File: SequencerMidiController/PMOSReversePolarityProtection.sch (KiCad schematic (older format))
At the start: 4 parts, among them Q1 HX2301A

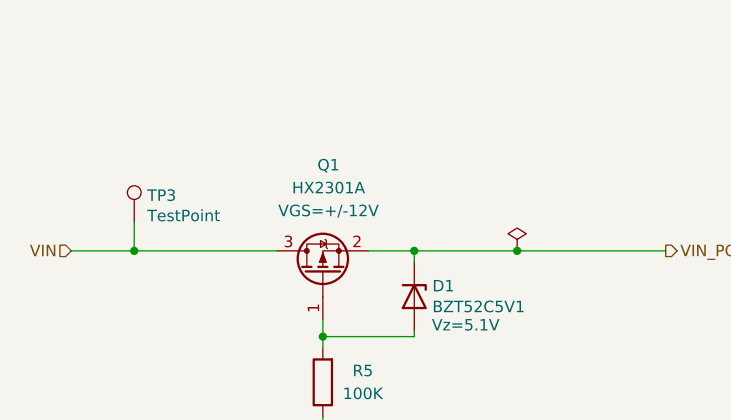
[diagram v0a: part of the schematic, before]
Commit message: RevA Layout draft completed
- Needs tidy up
- Add test points
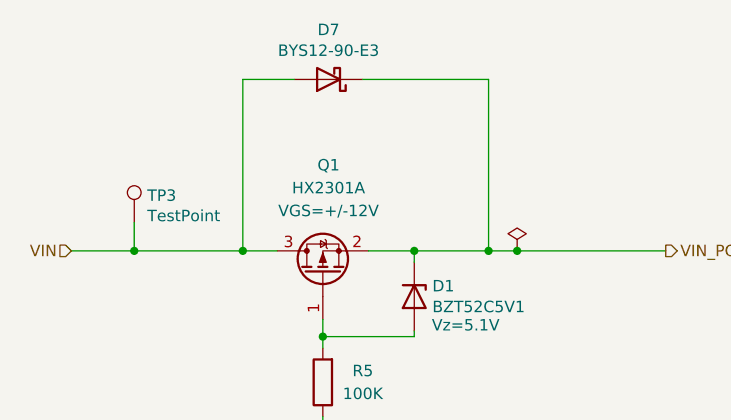
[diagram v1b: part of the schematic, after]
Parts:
- added D7: BYS12-90-E3, Diode_SMD:D_SMA, symbol Device:D_Schottky
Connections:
- net VIN: now also D7.2 (A)
- net VIN_POL: now also D7.1 (K)
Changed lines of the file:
@@
 Connection ~ 6100 2825
 Wire Wire Line
-	6100 2825 6550 2825
+	6100 2825 6425 2825
 Wire Wire Line
 	6100 2875 6100 2825
@@
 F 2 "Resistor_SMD:R_0805_2012Metric_Pad1.20x1.40mm_HandSolder" V 5630 3400 50  0001 C CNN
 F 3 "~" H 5700 3400 50  0001 C CNN
-F 4 "" V 5700 3400 50  0001 C CNN "Type"
-F 5 "" H 5700 3400 50  0001 C CNN "LcscNo"
+F 4 "~" V 5700 3400 50  0001 C CNN "Type"
+F 5 "~" H 5700 3400 50  0001 C CNN "LcscNo"
 	1    5700 3400
 	-1   0    0    1
@@
 $EndComp
 Wire Wire Line
-	5500 2825 4875 2825
+	5500 2825 5350 2825
 Text HLabel 4600 2825 0    50   Input ~ 0
 VIN
@@
 F 2 "TestPoint:TestPoint_Pad_1.0x1.0mm" H 5075 2700 50  0001 C CNN
 F 3 "~" H 5075 2700 50  0001 C CNN
+F 4 "~" H 4875 2700 50  0001 C CNN "LcscNo"
+F 5 "~" H 4875 2700 50  0001 C CNN "Type"
 	1    4875 2700
 	1    0    0    -1
@@
 Wire Wire Line
 	5700 3550 5700 3650
+$Comp
+L Device:D_Schottky D7
+U 1 1 634DDB6A
+P 5725 2075
+F 0 "D7" H 5725 1858 50  0000 C CNN
+F 1 "BYS12-90-E3" H 5725 1949 50  0000 C CNN
+F 2 "Diode_SMD:D_SMA" H 5725 2075 50  0001 C CNN
+F 3 "https://www.vishay.com/docs/88950/bys12-90.pdf" H 5725 2075 50  0001 C CNN
+	1    5725 2075
+	-1   0    0    1
+$EndComp
+Wire Wire Line
+	5575 2075 5350 2075
+Wire Wire Line
+	5350 2075 5350 2825
+Connection ~ 5350 2825
+Wire Wire Line
+	5350 2825 4875 2825
+Wire Wire Line
+	5875 2075 6425 2075
+Wire Wire Line
+	6425 2075 6425 2825
+Connection ~ 6425 2825
+Wire Wire Line
+	6425 2825 6550 2825
 $EndSCHEMATC

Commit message: Completed RevA layout
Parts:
- removed D7: BYS12-90-E3, Diode_SMD:D_SMA, symbol Device:D_Schottky
- D1: value BZT52C5V1 -> MMSZ4694T1G; LcscNo C353516 -> (none); Type Vz=5.1V -> (none)
- Q1: value HX2301A -> Si2323DS; symbol Transistor_FET:DMG2301L -> Device:Q_PMOS_GSD; Type VGS=+/-12V -> (none)
- R5: value 100K -> 100R
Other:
- note added: "RDS(ON) should be 100mΩ or less\nDrain current (4.5A) should be higher than 3A\nVDS (20V) should be higher than VIN (9V)"
- note added: "Zener Voltage should not exceed Q1 VGS limits"
- moved on the sheet: D1, Q1, R5, TP3
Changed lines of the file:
@@
 L power:PWR_FLAG #FLG?
 U 1 1 60B71BEE
-P 6550 2825
+P 8550 3825
 AR Path="/60B71BEE" Ref="#FLG?"  Part="1"
 AR Path="/5DEF0009/60B71BEE" Ref="#FLG?"  Part="1"
 AR Path="/60BD3123/60BD33F0/60B71BEE" Ref="#FLG0101"  Part="1"
-F 0 "#FLG0101" H 6550 2900 50  0001 C CNN
-F 1 "PWR_FLAG" H 6550 2996 50  0001 C CNN
-F 2 "" H 6550 2825 50  0001 C CNN
-F 3 "~" H 6550 2825 50  0001 C CNN
-	1    6550 2825
+F 0 "#FLG0101" H 8550 3900 50  0001 C CNN
+F 1 "PWR_FLAG" H 8550 3996 50  0001 C CNN
+F 2 "" H 8550 3825 50  0001 C CNN
+F 3 "~" H 8550 3825 50  0001 C CNN
+	1    8550 3825
 	1    0    0    -1
 $EndComp
-Connection ~ 6550 2825
+Connection ~ 8550 3825
 Wire Wire Line
-	6550 2825 7200 2825
+	8550 3825 9200 3825
 Wire Wire Line
-	5900 2825 6100 2825
-Connection ~ 6100 2825
+	5825 3825 6375 3825
+Connection ~ 6375 3825
 Wire Wire Line
-	6100 2825 6425 2825
+	6375 4125 6375 3825
 Wire Wire Line
-	6100 2875 6100 2825
+	5625 4450 5625 4125
+Connection ~ 5625 4450
 Wire Wire Line
-	5700 3200 5700 3125
-Connection ~ 5700 3200
+	6375 4450 5625 4450
 Wire Wire Line
-	6100 3200 5700 3200
-Wire Wire Line
-	6100 3175 6100 3200
+	6375 4425 6375 4450
 $Comp
 L Diode:BZT52Bxx D?
 U 1 1 60B71C00
-P 6100 3025
+P 6375 4275
 AR Path="/60B71C00" Ref="D?"  Part="1"
 AR Path="/5DEF0009/60B71C00" Ref="D?"  Part="1"
 AR Path="/60BD3123/60BD33F0/60B71C00" Ref="D1"  Part="1"
-F 0 "D1" V 6054 3104 50  0000 L CNN
-F 1 "BZT52C5V1" V 6145 3104 50  0000 L CNN
-F 2 "Diode_SMD:D_SOD-123" H 6100 2850 50  0001 C CNN
-F 3 "https://diotec.com/tl_files/diotec/files/pdf/datasheets/bzt52b2v4.pdf" H 6100 3025 50  0001 C CNN
-F 4 "Vz=5.1V" V 6225 3250 50  0000 C CNN "Type"
-F 5 "C353516" V 6100 3025 50  0001 C CNN "LcscNo"
-	1    6100 3025
+F 0 "D1" V 6329 4354 50  0000 L CNN
+F 1 "MMSZ4694T1G" V 6420 4354 50  0000 L CNN
+F 2 "Diode_SMD:D_SOD-123" H 6375 4100 50  0001 C CNN
+F 3 "https://www.onsemi.com/pdf/datasheet/mmsz4678t1-d.pdf" H 6375 4275 50  0001 C CNN
+F 4 "~" V 6500 4500 50  0001 C CNN "Type"
+F 5 "~" V 6375 4275 50  0001 C CNN "LcscNo"
+	1    6375 4275
 	0    1    1    0
 $EndComp
 Wire Wire Line
-	5700 3250 5700 3200
+	5625 4800 5625 4450
 $Comp
 L Device:R R?
 U 1 1 60B71C09
-P 5700 3400
+P 5625 4950
 AR Path="/60B71C09" Ref="R?"  Part="1"
 AR Path="/5DEF0009/60B71C09" Ref="R?"  Part="1"
 AR Path="/60BD3123/60BD33F0/60B71C09" Ref="R5"  Part="1"
-F 0 "R5" H 5525 3350 50  0000 C CNN
-F 1 "100K" H 5525 3450 50  0000 C CNN
-F 2 "Resistor_SMD:R_0805_2012Metric_Pad1.20x1.40mm_HandSolder" V 5630 3400 50  0001 C CNN
-F 3 "~" H 5700 3400 50  0001 C CNN
-F 4 "~" V 5700 3400 50  0001 C CNN "Type"
-F 5 "~" H 5700 3400 50  0001 C CNN "LcscNo"
-	1    5700 3400
+F 0 "R5" H 5450 4900 50  0000 C CNN
+F 1 "100R" H 5450 5000 50  0000 C CNN
+F 2 "Resistor_SMD:R_0805_2012Metric_Pad1.20x1.40mm_HandSolder" V 5555 4950 50  0001 C CNN
+F 3 "~" H 5625 4950 50  0001 C CNN
+F 4 "~" V 5625 4950 50  0001 C CNN "Type"
+F 5 "~" H 5625 4950 50  0001 C CNN "LcscNo"
+	1    5625 4950
 	-1   0    0    1
 $EndComp
@@
 L power:GNDS #PWR?
 U 1 1 60B71C10
-P 5700 3650
+P 5625 5200
 AR Path="/60B71C10" Ref="#PWR?"  Part="1"
 AR Path="/5DEF0009/60B71C10" Ref="#PWR?"  Part="1"
 AR Path="/60BD3123/60BD33F0/60B71C10" Ref="#PWR0107"  Part="1"
-F 0 "#PWR0107" H 5700 3400 50  0001 C CNN
-F 1 "GNDS" H 5705 3477 50  0000 C CNN
-F 2 "" H 5700 3650 50  0001 C CNN
-F 3 "" H 5700 3650 50  0001 C CNN
-	1    5700 3650
+F 0 "#PWR0107" H 5625 4950 50  0001 C CNN
+F 1 "GNDS" H 5630 5027 50  0000 C CNN
+F 2 "" H 5625 5200 50  0001 C CNN
+F 3 "" H 5625 5200 50  0001 C CNN
+	1    5625 5200
 	1    0    0    -1
 $EndComp
-Wire Wire Line
-	5500 2825 5350 2825
-Text HLabel 4600 2825 0    50   Input ~ 0
+Text HLabel 2250 3825 0    50   Input ~ 0
 VIN
 $Comp
 L Connector:TestPoint TP?
 U 1 1 60B71C23
-P 4875 2700
+P 2525 3700
 AR Path="/5DE5D23A/60B71C23" Ref="TP?"  Part="1"
 AR Path="/5DEF0009/60B71C23" Ref="TP?"  Part="1"
 AR Path="/60BD3123/60BD33F0/60B71C23" Ref="TP3"  Part="1"
-F 0 "TP3" H 4932 2817 50  0000 L CNN
-F 1 "TestPoint" H 4932 2728 50  0000 L CNN
-F 2 "TestPoint:TestPoint_Pad_1.0x1.0mm" H 5075 2700 50  0001 C CNN
-F 3 "~" H 5075 2700 50  0001 C CNN
-F 4 "~" H 4875 2700 50  0001 C CNN "LcscNo"
-F 5 "~" H 4875 2700 50  0001 C CNN "Type"
-	1    4875 2700
+F 0 "TP3" H 2582 3817 50  0000 L CNN
+F 1 "TestPoint" H 2582 3728 50  0000 L CNN
+F 2 "TestPoint:TestPoint_Pad_1.0x1.0mm" H 2725 3700 50  0001 C CNN
+F 3 "~" H 2725 3700 50  0001 C CNN
+F 4 "~" H 2525 3700 50  0001 C CNN "LcscNo"
+F 5 "~" H 2525 3700 50  0001 C CNN "Type"
+	1    2525 3700
 	1    0    0    -1
 $EndComp
 Wire Wire Line
-	4875 2700 4875 2825
-Connection ~ 4875 2825
+	2525 3700 2525 3825
+Connection ~ 2525 3825
 Wire Wire Line
-	4875 2825 4600 2825
+	2525 3825 2250 3825
+Text HLabel 9200 3825 2    50   Output ~ 0
+VIN_POL
+Wire Wire Line
+	5625 5100 5625 5200
+Text Notes 5125 3700 0    39   ~ 0
+RDS(ON) should be 100mΩ or less\nDrain current (4.5A) should be higher than 3A\nVDS (20V) should be higher than VIN (9V)
+Text Notes 6450 4525 0    39   ~ 0
+Zener Voltage should not exceed Q1 VGS limits
+Wire Wire Line
+	2525 3825 5425 3825
+Wire Wire Line
+	6375 3825 8550 3825
 $Comp
-L Transistor_FET:DMG2301L Q?
+L Device:Q_PMOS_GSD Q?
 U 1 1 60B71C2E
-P 5700 2925
+P 5625 3925
 AR Path="/5DEF0009/60B71C2E" Ref="Q?"  Part="1"
 AR Path="/60B6D227/60B71C2E" Ref="Q?"  Part="1"
 AR Path="/60BD3123/60BD33F0/60B71C2E" Ref="Q1"  Part="1"
-F 0 "Q1" V 6175 2900 50  0000 C CNN
-F 1 "HX2301A" V 6075 2900 50  0000 C CNN
-F 2 "Package_TO_SOT_SMD:SOT-23" H 5900 2850 50  0001 L CIN
-F 3 "https://datasheet.lcsc.com/szlcsc/1912111437_HX-hengjiaxing-HX2301A_C296298.pdf" H 5700 2925 50  0001 L CNN
-F 4 "VGS=+/-12V" V 5975 2900 50  0000 C CNN "Type"
-F 5 "C296298" V 5700 2925 50  0001 C CNN "LcscNo"
-	1    5700 2925
+F 0 "Q1" V 6250 3900 50  0000 C CNN
+F 1 "Si2323DS" V 6150 3900 50  0000 C CNN
+F 2 "Package_TO_SOT_SMD:SOT-23" H 5825 3850 50  0001 L CIN
+F 3 "https://www.vishay.com/docs/64004/si2323dds.pdf" H 5625 3925 50  0001 L CNN
+F 4 "~" V 6050 3900 50  0000 C CNN "Type"
+F 5 "C296298" V 5625 3925 50  0001 C CNN "LcscNo"
+	1    5625 3925
 	0    -1   -1   0
 $EndComp
-Text HLabel 7200 2825 2    50   Output ~ 0
-VIN_POL
-Wire Wire Line
-	5700 3550 5700 3650
-$Comp
-L Device:D_Schottky D7
-U 1 1 634DDB6A
-P 5725 2075
-F 0 "D7" H 5725 1858 50  0000 C CNN
-F 1 "BYS12-90-E3" H 5725 1949 50  0000 C CNN
-F 2 "Diode_SMD:D_SMA" H 5725 2075 50  0001 C CNN
-F 3 "https://www.vishay.com/docs/88950/bys12-90.pdf" H 5725 2075 50  0001 C CNN
-	1    5725 2075
-	-1   0    0    1
-$EndComp
-Wire Wire Line
-	5575 2075 5350 2075
-Wire Wire Line
-	5350 2075 5350 2825
-Connection ~ 5350 2825
-Wire Wire Line
-	5350 2825 4875 2825
-Wire Wire Line
-	5875 2075 6425 2075
-Wire Wire Line
-	6425 2075 6425 2825
-Connection ~ 6425 2825
-Wire Wire Line
-	6425 2825 6550 2825
 $EndSCHEMATC

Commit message: updated
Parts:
- added D7: RED, LED_SMD:LED_0805_2012Metric_Pad1.15x1.40mm_HandSolder, symbol Device:LED
- added R13: 2K2, Resistor_SMD:R_0805_2012Metric_Pad1.20x1.40mm_HandSolder, symbol Device:R
- R5: footprint Resistor_SMD:R_0805_2012Metric_Pad1.20x1.40mm_HandSolder -> Resistor_SMD:R_1206_3216Metric_Pad1.30x1.75mm_HandSolder
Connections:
- net GNDS: now also R13.2
- net VIN_POL: now also D7.2 (A)
- new net: D7.1 (K), R13.1
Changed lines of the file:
@@
 F 0 "R5" H 5450 4900 50  0000 C CNN
 F 1 "100R" H 5450 5000 50  0000 C CNN
-F 2 "Resistor_SMD:R_0805_2012Metric_Pad1.20x1.40mm_HandSolder" V 5555 4950 50  0001 C CNN
+F 2 "Resistor_SMD:R_1206_3216Metric_Pad1.30x1.75mm_HandSolder" V 5555 4950 50  0001 C CNN
 F 3 "~" H 5625 4950 50  0001 C CNN
 F 4 "~" V 5625 4950 50  0001 C CNN "Type"
@@
 L power:GNDS #PWR?
 U 1 1 60B71C10
-P 5625 5200
+P 5625 5375
 AR Path="/60B71C10" Ref="#PWR?"  Part="1"
 AR Path="/5DEF0009/60B71C10" Ref="#PWR?"  Part="1"
 AR Path="/60BD3123/60BD33F0/60B71C10" Ref="#PWR0107"  Part="1"
-F 0 "#PWR0107" H 5625 4950 50  0001 C CNN
-F 1 "GNDS" H 5630 5027 50  0000 C CNN
-F 2 "" H 5625 5200 50  0001 C CNN
-F 3 "" H 5625 5200 50  0001 C CNN
-	1    5625 5200
+F 0 "#PWR0107" H 5625 5125 50  0001 C CNN
+F 1 "GNDS" H 5630 5202 50  0000 C CNN
+F 2 "" H 5625 5375 50  0001 C CNN
+F 3 "" H 5625 5375 50  0001 C CNN
+	1    5625 5375
 	1    0    0    -1
 $EndComp
@@
 VIN_POL
 Wire Wire Line
-	5625 5100 5625 5200
+	5625 5100 5625 5175
 Text Notes 5125 3700 0    39   ~ 0
 RDS(ON) should be 100mΩ or less\nDrain current (4.5A) should be higher than 3A\nVDS (20V) should be higher than VIN (9V)
@@
 	2525 3825 5425 3825
 Wire Wire Line
-	6375 3825 8550 3825
+	6375 3825 8425 3825
 $Comp
 L Device:Q_PMOS_GSD Q?
@@
 	0    -1   -1   0
 $EndComp
+$Comp
+L Device:LED D?
+U 1 1 60BF64D6
+P 8425 4150
+AR Path="/60BD3123/60BD5AA5/60BF64D6" Ref="D?"  Part="1"
+AR Path="/60BD3123/63615DFB/60BF64D6" Ref="D?"  Part="1"
+AR Path="/60BD3123/60BD33F0/60BF64D6" Ref="D7"  Part="1"
+F 0 "D7" V 8464 4032 50  0000 R CNN
+F 1 "RED" V 8373 4032 50  0000 R CNN
+F 2 "LED_SMD:LED_0805_2012Metric_Pad1.15x1.40mm_HandSolder" H 8425 4150 50  0001 C CNN
+F 3 "~" H 8425 4150 50  0001 C CNN
+F 4 "C2293" H 8425 4150 50  0001 C CNN "LcscNo"
+F 5 "~" H 8425 4150 50  0001 C CNN "Type"
+	1    8425 4150
+	0    -1   -1   0
+$EndComp
+$Comp
+L Device:R R?
+U 1 1 60BF64DE
+P 8425 4625
+AR Path="/60BD3123/60BD5AA5/60BF64DE" Ref="R?"  Part="1"
+AR Path="/60BD3123/63615DFB/60BF64DE" Ref="R?"  Part="1"
+AR Path="/60BD3123/60BD33F0/60BF64DE" Ref="R13"  Part="1"
+F 0 "R13" H 8495 4671 50  0000 L CNN
+F 1 "2K2" H 8495 4580 50  0000 L CNN
+F 2 "Resistor_SMD:R_0805_2012Metric_Pad1.20x1.40mm_HandSolder" V 8355 4625 50  0001 C CNN
+F 3 "~" H 8425 4625 50  0001 C CNN
+F 4 "~" H 8425 4625 50  0001 C CNN "LcscNo"
+F 5 "~" H 8425 4625 50  0001 C CNN "Type"
+	1    8425 4625
+	1    0    0    -1
+$EndComp
+Wire Wire Line
+	8425 4475 8425 4300
+Wire Wire Line
+	8425 4000 8425 3825
+Wire Wire Line
+	8425 5175 5625 5175
+Wire Wire Line
+	8425 4775 8425 5175
+Connection ~ 5625 5175
+Wire Wire Line
+	5625 5175 5625 5375
+Connection ~ 8425 3825
+Wire Wire Line
+	8425 3825 8550 3825
 $EndSCHEMATC
